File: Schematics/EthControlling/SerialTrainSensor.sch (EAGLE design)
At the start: 17 parts, among them IC2 LMV358

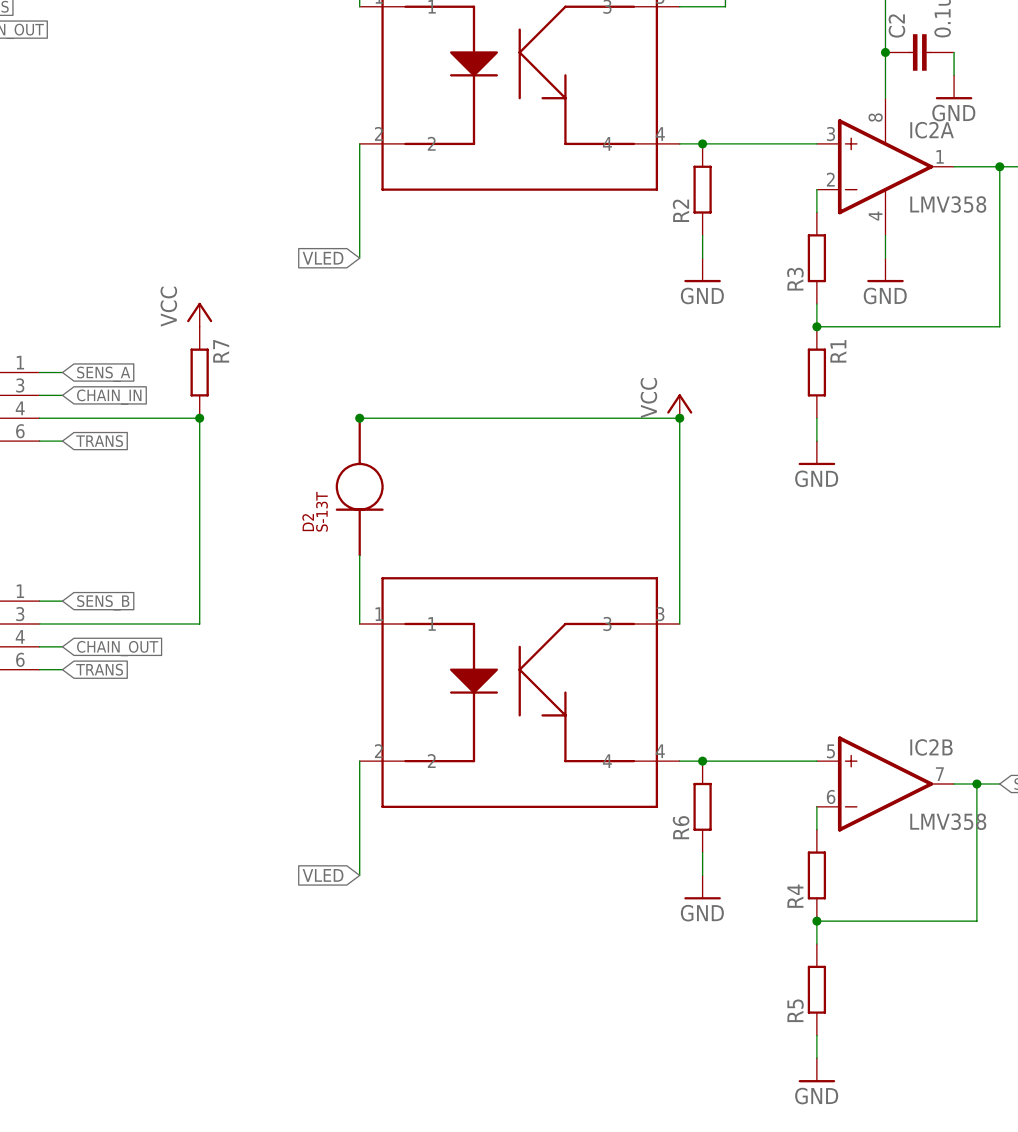
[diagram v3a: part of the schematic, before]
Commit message: debuging device transfer
Signed-off-by: sosoru <siva6991@yahoo.co.jp>
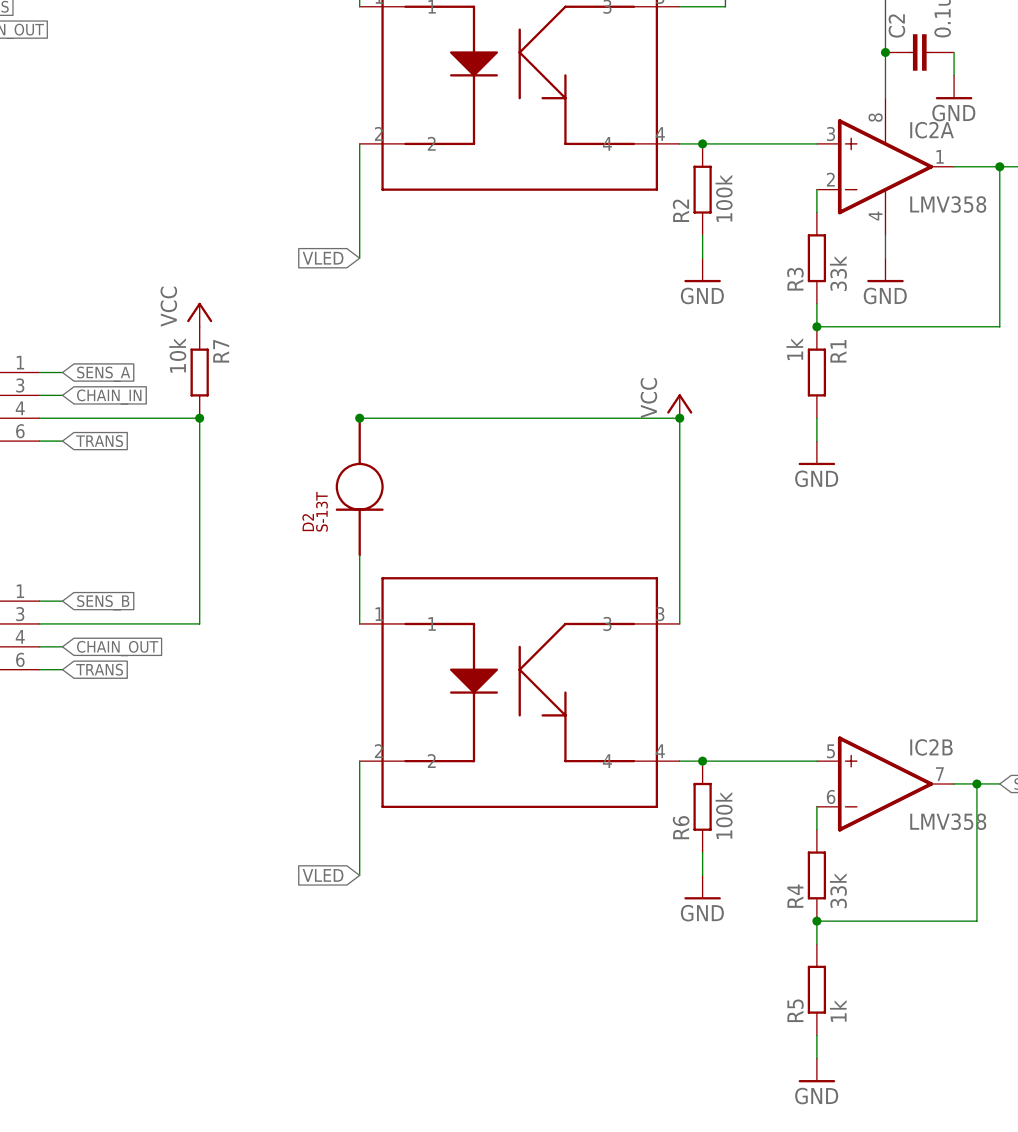
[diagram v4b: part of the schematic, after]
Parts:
- R1, R5: value (none) -> 1k
- R2, R6: value (none) -> 100k
- R3, R4: value (none) -> 33k
- R7: value (none) -> 10k
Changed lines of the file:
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@@
 <part name="D2" library="myparts" deviceset="S-1*3T" device=""/>
 <part name="GND7" library="supply1" deviceset="GND" device=""/>
-<part name="R3" library="rcl" deviceset="R-EU_" device="R0603"/>
-<part name="R1" library="rcl" deviceset="R-EU_" device="R0603"/>
+<part name="R3" library="rcl" deviceset="R-EU_" device="R0603" value="33k"/>
+<part name="R1" library="rcl" deviceset="R-EU_" device="R0603" value="1k"/>
 <part name="GND8" library="supply1" deviceset="GND" device=""/>
-<part name="R2" library="rcl" deviceset="R-EU_" device="R0603"/>
+<part name="R2" library="rcl" deviceset="R-EU_" device="R0603" value="100k"/>
 <part name="GND9" library="supply1" deviceset="GND" device=""/>
-<part name="R6" library="rcl" deviceset="R-EU_" device="R0603"/>
+<part name="R6" library="rcl" deviceset="R-EU_" device="R0603" value="100k"/>
 <part name="GND10" library="supply1" deviceset="GND" device=""/>
-<part name="R4" library="rcl" deviceset="R-EU_" device="R0603"/>
-<part name="R5" library="rcl" deviceset="R-EU_" device="R0603"/>
+<part name="R4" library="rcl" deviceset="R-EU_" device="R0603" value="33k"/>
+<part name="R5" library="rcl" deviceset="R-EU_" device="R0603" value="1k"/>
 <part name="GND11" library="supply1" deviceset="GND" device=""/>
 <part name="P+1" library="supply1" deviceset="VCC" device=""/>
@@
 <part name="SMD1" library="myparts" deviceset="SERIAL_SENSOR" device="HALF"/>
 <part name="SMD2" library="myparts" deviceset="SERIAL_SENSOR" device="HALF"/>
-<part name="R7" library="rcl" deviceset="R-EU_" device="R0603"/>
+<part name="R7" library="rcl" deviceset="R-EU_" device="R0603" value="10k"/>
 <part name="P+2" library="supply1" deviceset="VCC" device=""/>
 </parts>

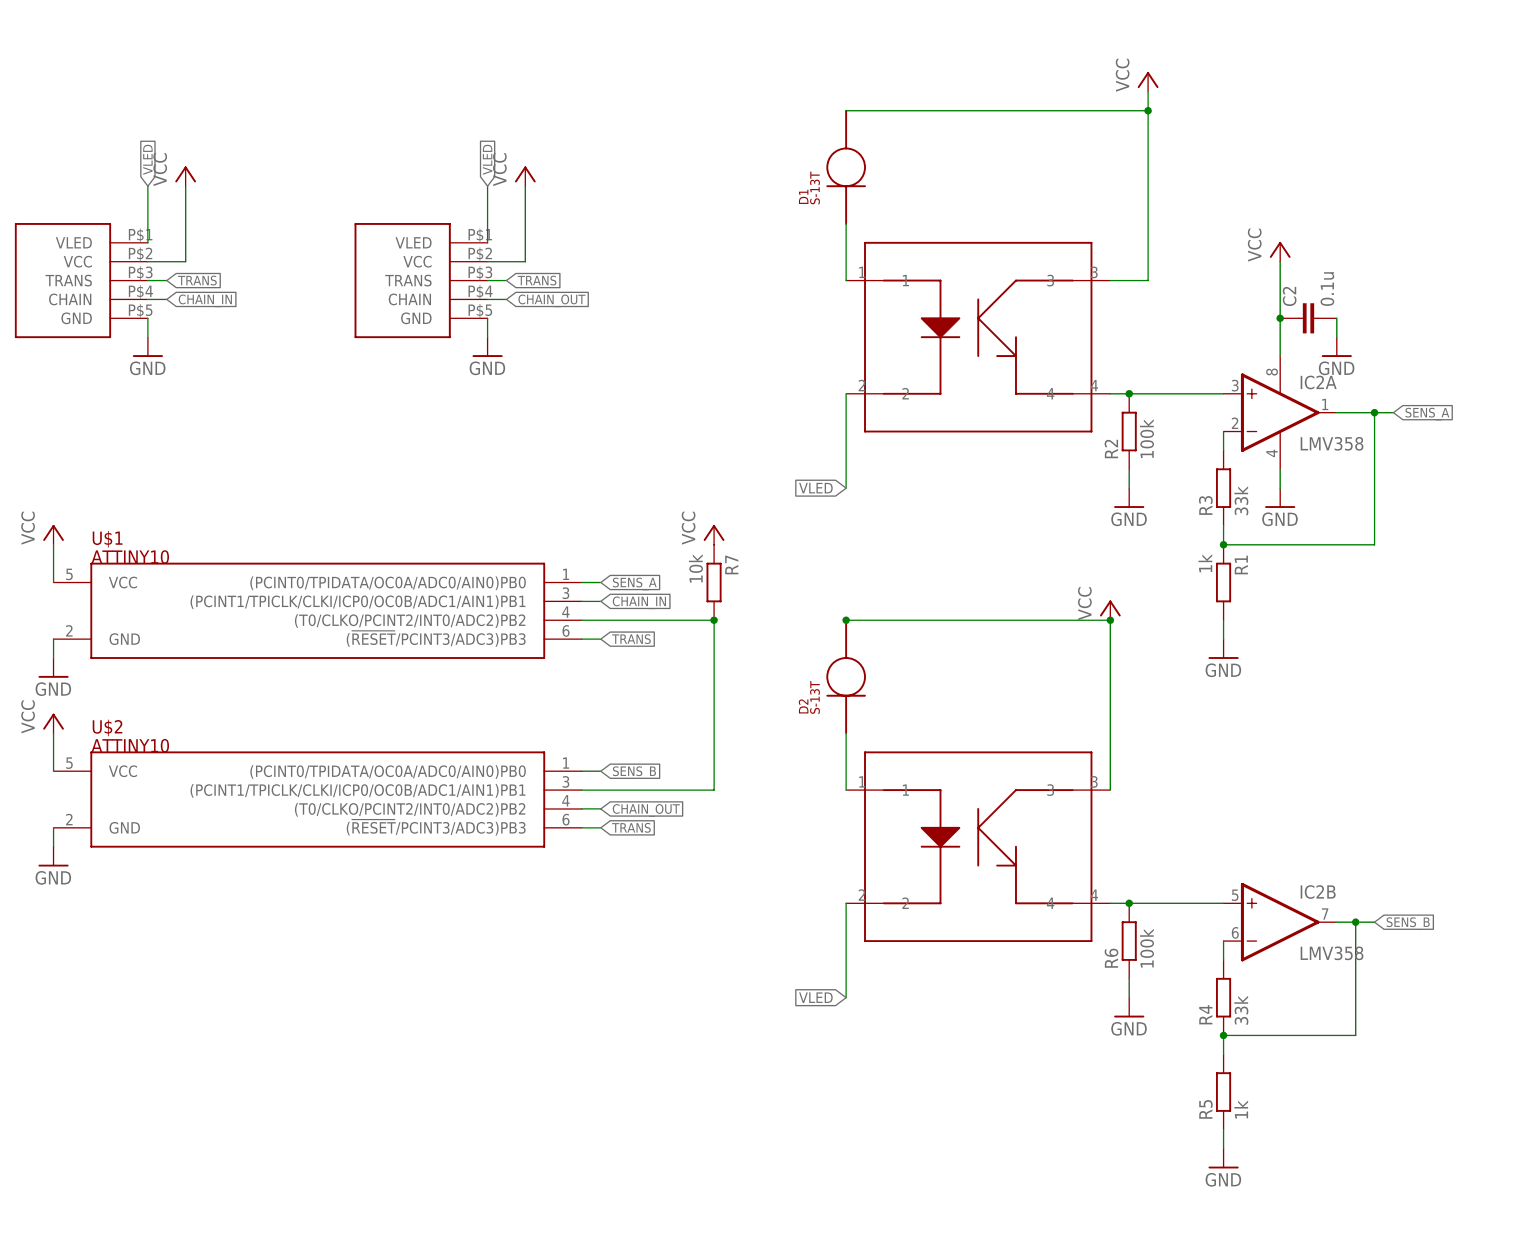
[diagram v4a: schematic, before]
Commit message: fixed train sensor board
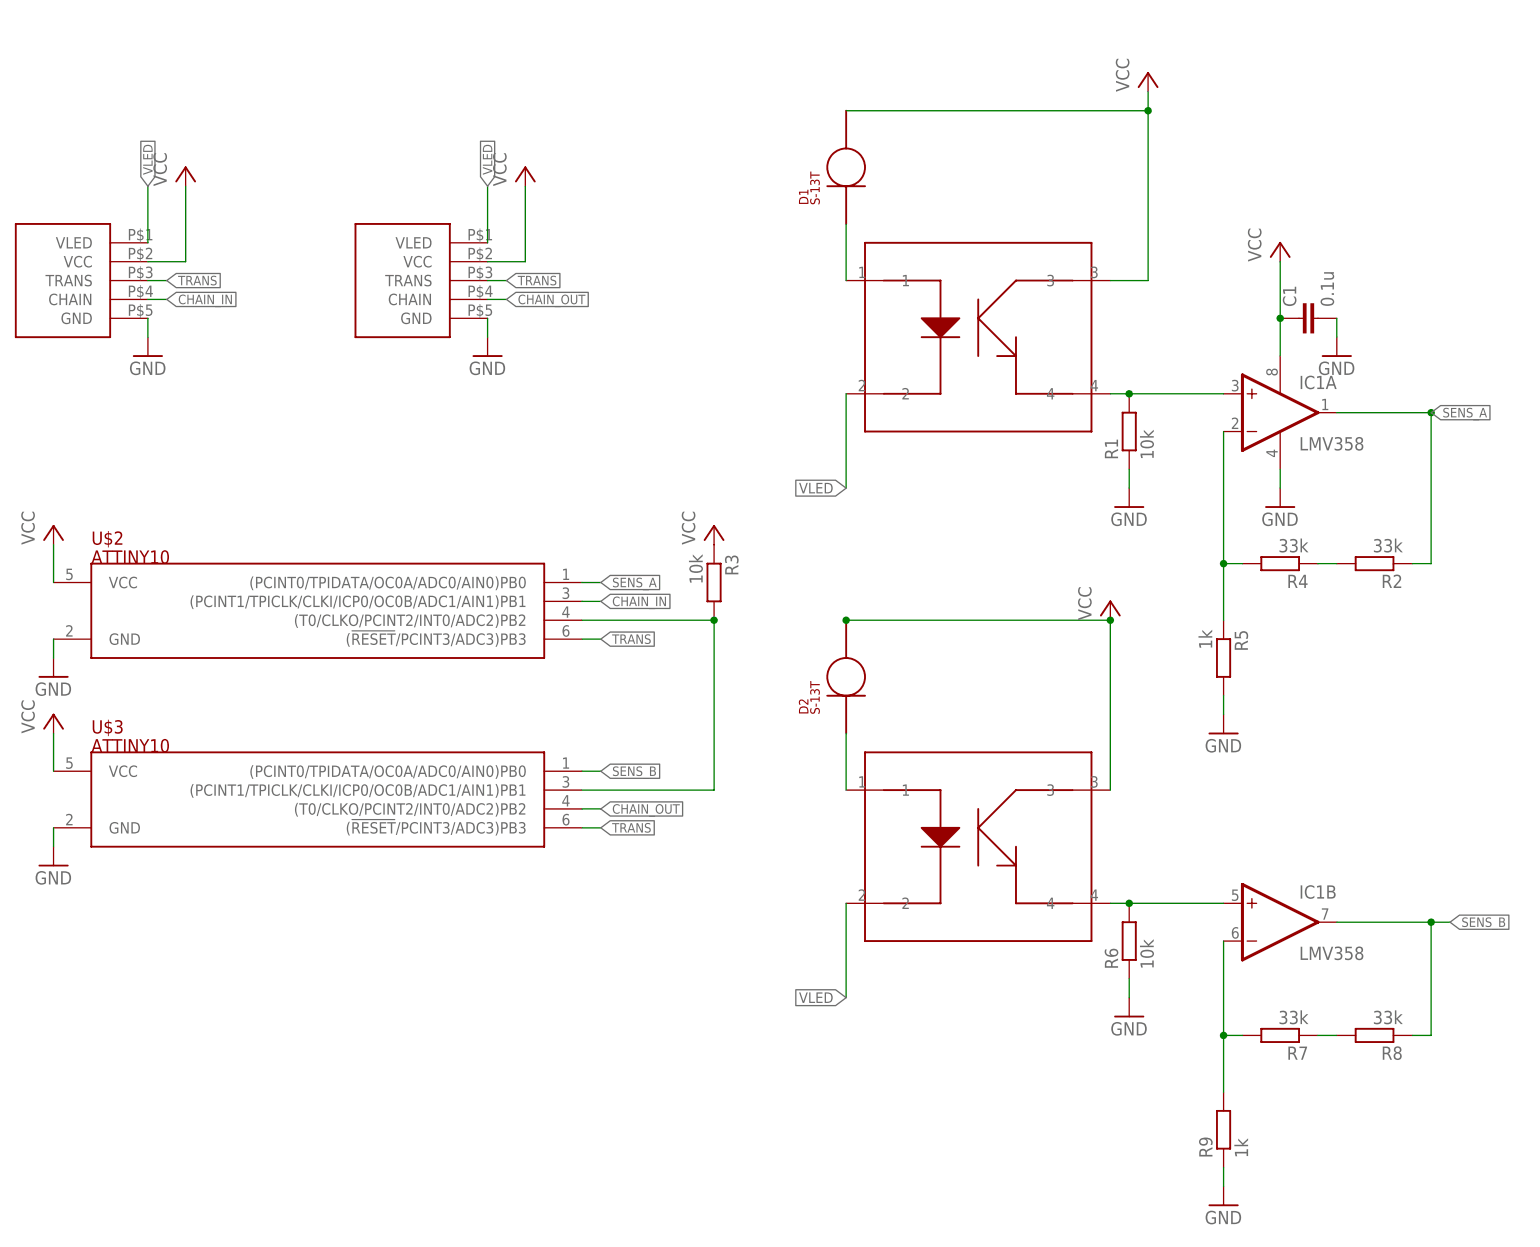
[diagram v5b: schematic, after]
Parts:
- removed U$101: TPR-105F, myparts:TPR-105F
- added R8: 33k, rcl:R-EU_R0603
- added R9: 1k, rcl:R-EU_R0603
- added U$3: ATTINY10, myparts:ATTINY10
- R1: value 1k -> 10k
- R2: value 100k -> 33k
- R3: value 33k -> 10k
- R6: value 100k -> 10k
- R7: value 10k -> 33k
- U$1: value ATTINY10 -> TPR-105F; device myparts:ATTINY10 -> myparts:TPR-105F
- renumbered C2 to C1, IC2 to IC1, U$100 to U$4
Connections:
- new net N$8: R2.2, R4.1
- new net N$9: R7.1, R8.2
- net CHAIN_IN: now also U$2.(PCINT1/TPICLK/CLKI/ICP0/OC0B/ADC1/AIN1)PB1; no longer U$1.(PCINT1/TPICLK/CLKI/ICP0/OC0B/ADC1/AIN1)PB1
- net CHAIN_OUT: now also U$3.(T0/CLKO/PCINT2/INT0/ADC2)PB2; no longer U$2.(T0/CLKO/PCINT2/INT0/ADC2)PB2
- net GND: now also R1.1, R5.2, R9.1, U$3.GND; no longer R1.2, R2.1, R5.1, U$1.GND
- net N$1: now also U$1.1; no longer U$101.1
- net N$2: now also R1.2, U$1.4; no longer R2.2, U$101.4
- net N$4: now also R3.2, U$2.(T0/CLKO/PCINT2/INT0/ADC2)PB2, U$3.(PCINT1/TPICLK/CLKI/ICP0/OC0B/ADC1/AIN1)PB1; no longer R7.2, U$1.(T0/CLKO/PCINT2/INT0/ADC2)PB2, U$2.(PCINT1/TPICLK/CLKI/ICP0/OC0B/ADC1/AIN1)PB1
- net N$6: now also R4.2, R5.1; no longer R3.2
- net N$7: now also R7.2, R9.2; no longer R4.2
- net SENS_A: now also R2.1, U$2.(PCINT0/TPIDATA/OC0A/ADC0/AIN0)PB0; no longer R1.1, R3.1, U$1.(PCINT0/TPIDATA/OC0A/ADC0/AIN0)PB0
- net SENS_B: now also R8.1, U$3.(PCINT0/TPIDATA/OC0A/ADC0/AIN0)PB0; no longer R4.1, R5.2, U$2.(PCINT0/TPIDATA/OC0A/ADC0/AIN0)PB0
- net TRANS: now also U$3.(!RESET!/PCINT3/ADC3)PB3; no longer U$1.(!RESET!/PCINT3/ADC3)PB3
- net VCC: now also R3.1, U$1.3, U$3.VCC; no longer R7.1, U$1.VCC, U$101.3
- net VLED: now also U$1.2; no longer U$101.2
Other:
- moved on the sheet: R1, R2, R3, R4, R5, R7, U$2

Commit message: ditto
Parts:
- R1, R6: value 10k -> 1k
- R2, R8: value 33k -> 3.3k
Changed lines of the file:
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@@
 <part name="D2" library="myparts" deviceset="S-1*3T" device=""/>
 <part name="GND7" library="supply1" deviceset="GND" device=""/>
-<part name="R2" library="rcl" deviceset="R-EU_" device="R0603" value="33k"/>
+<part name="R2" library="rcl" deviceset="R-EU_" device="R0603" value="3.3k"/>
 <part name="R5" library="rcl" deviceset="R-EU_" device="R0603" value="1k"/>
 <part name="GND8" library="supply1" deviceset="GND" device=""/>
-<part name="R1" library="rcl" deviceset="R-EU_" device="R0603" value="10k"/>
+<part name="R1" library="rcl" deviceset="R-EU_" device="R0603" value="1k"/>
 <part name="GND9" library="supply1" deviceset="GND" device=""/>
-<part name="R6" library="rcl" deviceset="R-EU_" device="R0603" value="10k"/>
+<part name="R6" library="rcl" deviceset="R-EU_" device="R0603" value="1k"/>
 <part name="GND10" library="supply1" deviceset="GND" device=""/>
 <part name="R7" library="rcl" deviceset="R-EU_" device="R0603" value="33k"/>
@@
 <part name="P+2" library="supply1" deviceset="VCC" device=""/>
 <part name="R4" library="rcl" deviceset="R-EU_" device="R0603" value="33k"/>
-<part name="R8" library="rcl" deviceset="R-EU_" device="R0603" value="33k"/>
+<part name="R8" library="rcl" deviceset="R-EU_" device="R0603" value="3.3k"/>
 </parts>
 <sheets>

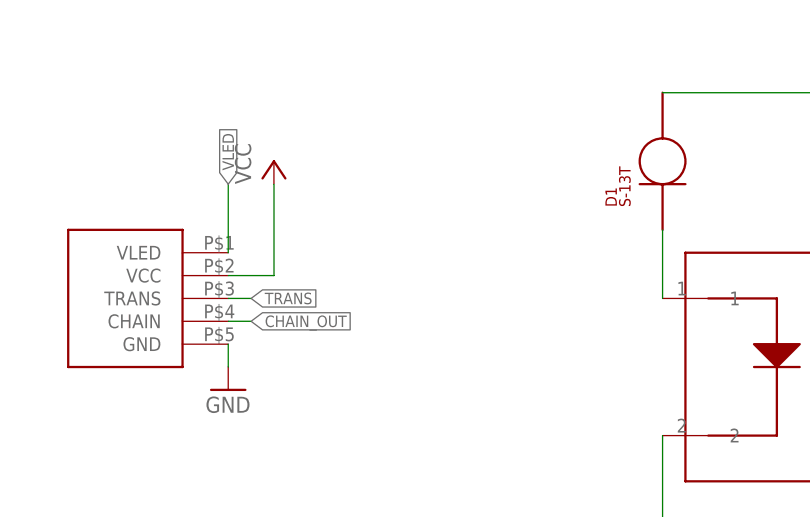
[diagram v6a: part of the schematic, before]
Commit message: add a resistor to transfer on TrSensor
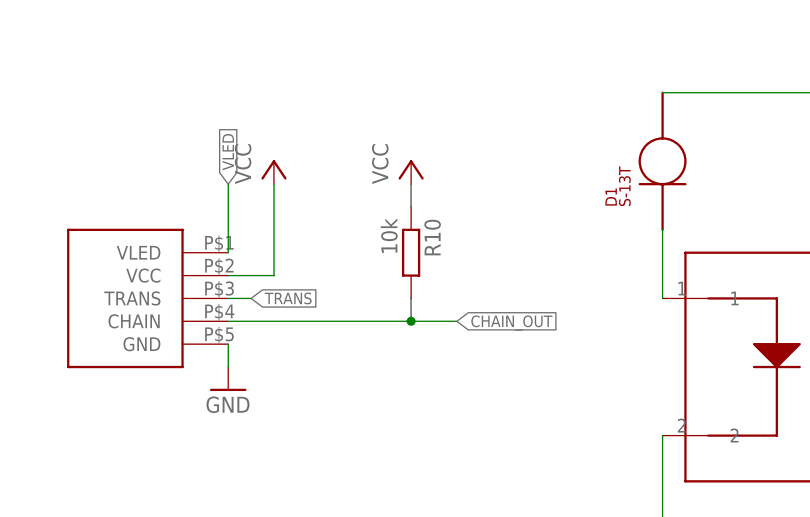
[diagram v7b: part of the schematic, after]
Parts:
- added R10: 10k, rcl:R-EU_R0603
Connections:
- net CHAIN_OUT: now also R10.2
- net VCC: now also R10.1
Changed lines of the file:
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@@
 <part name="R4" library="rcl" deviceset="R-EU_" device="R0603" value="33k"/>
 <part name="R8" library="rcl" deviceset="R-EU_" device="R0603" value="3.3k"/>
+<part name="P+5" library="supply1" deviceset="VCC" device=""/>
+<part name="R10" library="rcl" deviceset="R-EU_" device="R0603" value="10k"/>
 </parts>
 <sheets>
@@
 <instance part="R4" gate="G$1" x="167.64" y="63.5" rot="R180"/>
 <instance part="R8" gate="G$1" x="180.34" y="0" rot="R180"/>
+<instance part="P+5" gate="VCC" x="81.28" y="116.84"/>
+<instance part="R10" gate="G$1" x="81.28" y="106.68" rot="R270"/>
 </instances>
 <busses>
@@
 <net name="CHAIN_OUT" class="0">
 <segment>
-<wire x1="60.96" y1="99.06" x2="63.5" y2="99.06" width="0.1524" layer="91"/>
-<label x="63.5" y="99.06" size="1.27" layer="95" xref="yes"/>
+<wire x1="60.96" y1="99.06" x2="81.28" y2="99.06" width="0.1524" layer="91"/>
+<label x="86.36" y="99.06" size="1.27" layer="95" xref="yes"/>
 <pinref part="SMD2" gate="G$1" pin="CHAIN"/>
+<pinref part="R10" gate="G$1" pin="2"/>
+<wire x1="81.28" y1="99.06" x2="86.36" y2="99.06" width="0.1524" layer="91"/>
+<wire x1="81.28" y1="101.6" x2="81.28" y2="99.06" width="0.1524" layer="91"/>
+<junction x="81.28" y="99.06"/>
 </segment>
 <segment>
@@
 <pinref part="P+2" gate="VCC" pin="VCC"/>
 </segment>
-</net>
+<segment>
+<pinref part="P+5" gate="VCC" pin="VCC"/>
+<pinref part="R10" gate="G$1" pin="1"/>
+<wire x1="81.28" y1="114.3" x2="81.28" y2="111.76" width="0.1524" layer="91"/>
+</segment>
+</net>
